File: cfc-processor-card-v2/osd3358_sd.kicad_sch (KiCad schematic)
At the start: 77 parts, among them J100 DM3BT-DSF-PEJS, U11 TCAN330, U17 25AAXX, U2 DS90CR218AMTD/NOPBMTD48_TEX-L, U3 THGBMJG7C2LBAU8, U7 OSD3358-512M-BSM

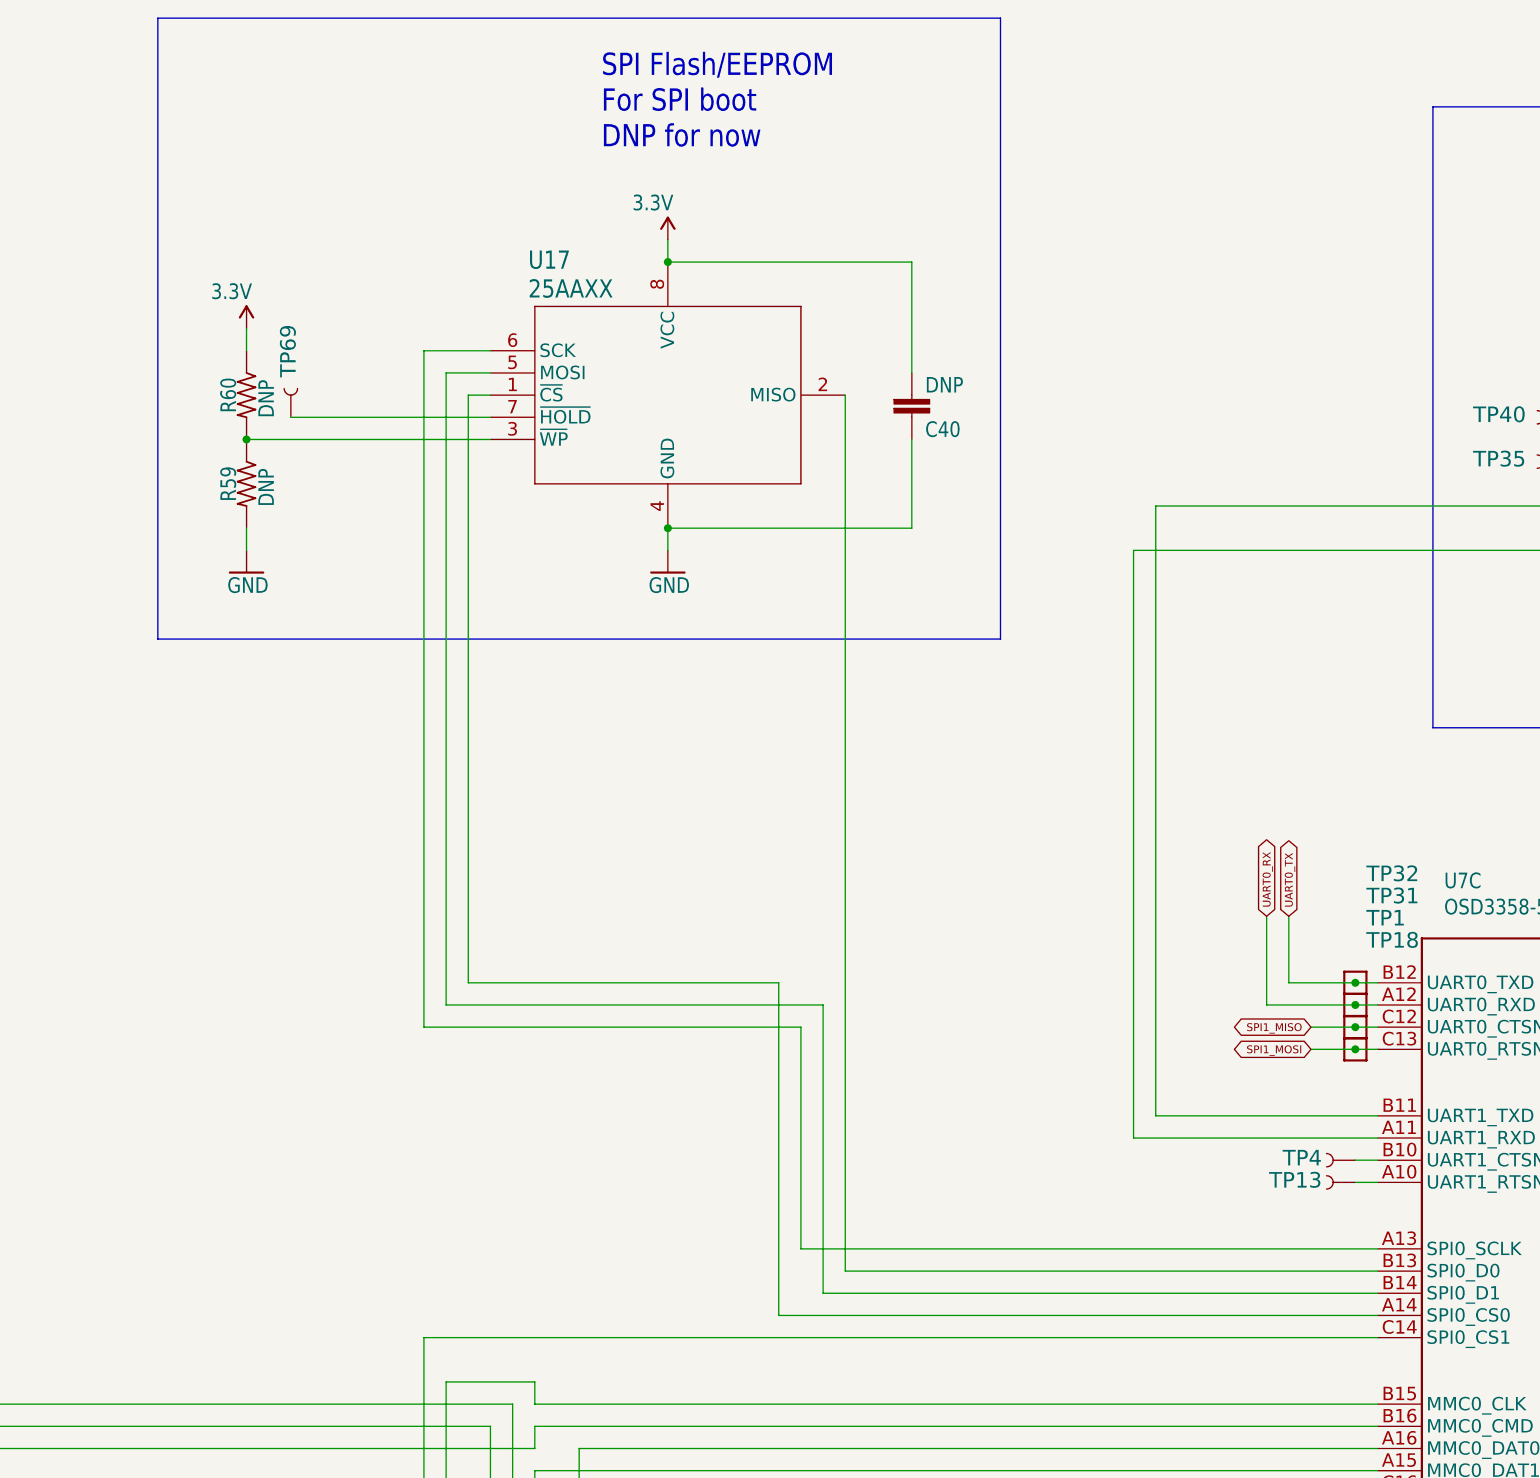
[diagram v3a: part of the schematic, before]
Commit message: More layout polishing Removed unused SPI EEPROM.
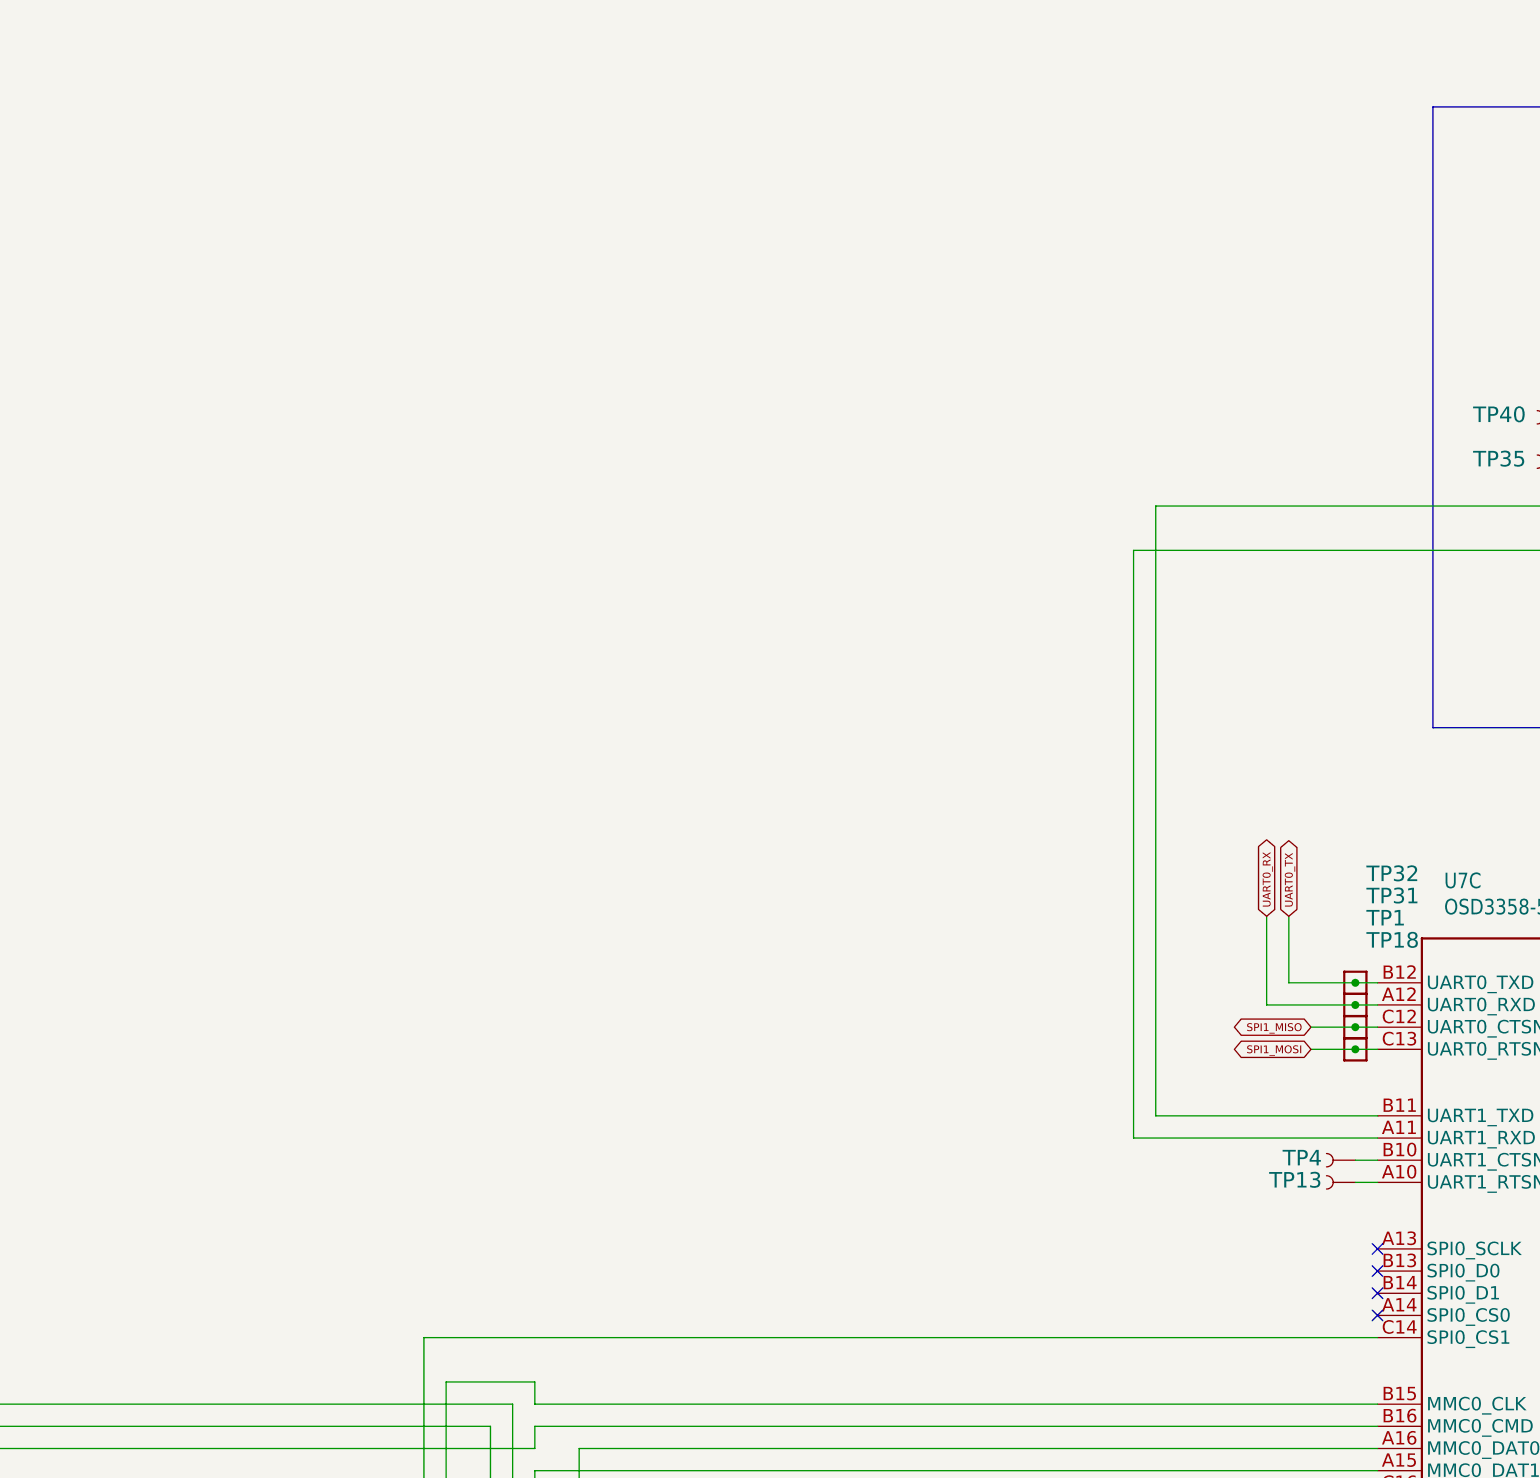
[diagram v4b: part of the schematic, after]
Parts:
- removed C40: DNP, oresat-passives:0603-C-NOSILK, symbol cfc-card-eagle-import:C-EU0603-A
- removed R59, R60: DNP, oresat-passives:0603-C-NOSILK, symbol cfc-card-eagle-import:R-US_0603-A
- removed TP69: TEST-POINT3X4, cfc-card:PAD.03X.04, symbol cfc-card-eagle-import:TEST-POINT3X4
- removed U17: 25AAXX, cfc-card:SOIC8, symbol cfc-card-eagle-import:25AAXX
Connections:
- no-connect marks 44 -> 48
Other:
- note removed: "SPI Flash/EEPROM For SPI boot DNP for now"

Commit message: Final polish on schematic and PCB. Cleaned up BOM, fixed github issues which were not really issues. Lots of BOM cleanup, with MPNs and DPNs.
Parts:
- removed TP33, TP34: TEST-POINT, cfc-card:2MM-TEST-POINT, symbol cfc-card-eagle-import:TEST-POINT
- added TP10, TP11, TP14, TP9: TEST-POINT3X4, cfc-card:PAD.03X.04, symbol cfc-card-eagle-import:TEST-POINT3X4
- C1, C16, C17, C20, C28, C7: DIS Digi-Key -> DigiKey; DPN 490-6350-1-ND -> 399-C0402C102J3GACAUTOCT-ND; MFR Murata -> KEMET; MPN GRM155R71H102KA01J -> C0402C102J3GACAUTO
- C10, C12, C3, C5, C6, C9: value 1uF -> 1u; DIS (none) -> DigiKey; DPN (none) -> 587-3473-1-ND; MFR (none) -> Taiyo Yuden; MPN (none) -> TMK107BJ105KAHT
- C11, C31: value 0.1uF -> 100n; DIS (none) -> DigiKey; DPN (none) -> 587-3472-1-ND; MFR (none) -> Taiyo Yuden; MPN (none) -> TMK107BJ104KAHT
- C2, C8: value 10uF -> 10u; DIS (none) -> DigiKey; DPN (none) -> 490-GRT21BC71E106KE13LCT-ND; MFR (none) -> Murata Electronics; MPN (none) -> GRT21BC71E106KE13L
- C21, C23, C24, C25, C26, C27: DIS Digi-Key -> DigiKey; DPN 399-7842-1-ND -> 399-C0402C100F5GACAUTOCT-ND; MFR Kemet -> KEMET; MPN C0603C103M5RACTU -> C0402C100F5GACAUTO
- C42, C43, C45, C46, C47, C48: DIS Digi-Key -> DigiKey; DPN 399-1177-1-ND -> 399-17167-1-ND; MFR Kemet -> KEMET; MPN C0805C104Z5VACTU -> C0402C104K4RECAUTO
- C49: footprint oresat-passives:0603-C-NOSILK -> oresat-passives:0805-C-NOSILK; DIS Digi-Key -> DigiKey; DPN 490-14372-1-ND -> 490-GRT21BC71E106KE13LCT-ND; MFR Murata -> Murata Electronics; MPN GRM188R61A106KE69J -> GRT21BC71E106KE13L
- D2, D3, D4, D5: footprint cfc-card:LED-0603 -> LED_SMD:LED_0603_1608Metric; symbol cfc-card-eagle-import:LED-BLUE0603 -> Device:LED_Small; DIS (none) -> DigiKey; DPN (none) -> 732-4966-1-ND; MFR (none) -> Wurth; MPN (none) -> 150060BS75000
- J6: renamed from J100; footprint cfc-card:DM3BT-DSF-PEJS -> oresat-connectors:J-Hirose-DM3BT-DSF-PEJS; symbol cfc-card-eagle-import:DM3BT-DSF-PEJS -> oresat-connectors:DM3BT-DSF-PEJS; DIS (none) -> DigiKey; DPN (none) -> HR1942CT-ND; MFR (none) -> Hirose; MPN (none) -> DM3BT-DSF-PEJS
- JP1, TP1, TP13, TP18, TP19, TP20, TP21, TP22, TP23, TP24, TP26, TP27, TP28, TP29, TP30, TP31, TP32, TP35, TP4, TP40: now left out of the parts list
- R11: value DNP -> 10k; now not fitted
- R2, R3, R4, R5: DIS (none) -> DigiKey; DPN (none) -> RMCF0603FT1K00CT-ND; MFR (none) -> Stackpole Electronics Inc; MPN (none) -> RMCF0603FT1K00
- R29, R30: value NP -> 100; now not fitted
- R6, R7: DIS Dgi-Key -> DigiKey; DPN 311-100MCT-ND -> RMCF0402FT100RCT-ND; MFR Yageo -> Stackpole Electronics Inc; MPN RC0201FR-07100RL -> RMCF0402FT100R
- RA1: renamed from R8; DIS (none) -> DigiKey; MFR (none) -> Panasonic Electronic Components; MPN (none) -> EXB-A10P103J
- RA2: renamed from R9; DIS (none) -> DigiKey; MFR (none) -> Panasonic Electronic Components; MPN (none) -> EXB-A10P103J
- RA3: renamed from R10; DIS (none) -> DigiKey; MFR (none) -> Panasonic Electronic Components; MPN (none) -> EXB-A10P103J
- U11: footprint cfc-card:SOT23-8_TI-DCN -> Package_TO_SOT_SMD:SOT-23-8; symbol cfc-card-eagle-import:TCAN330 -> oresat-ics:TCAN330; DIS (none) -> DigiKey; DPN (none) -> 296-44211-1-ND; MFR (none) -> Texas Instruments; MPN (none) -> TCAN330GDCNT
- U2: value DS90CR218AMTD/NOPBMTD48_TEX-L -> DS90CR218AMTD/NOPB; DIS (none) -> DigiKey; DPN (none) -> DS90CR218AMTD/NOPB-ND; MFR (none) -> Texas Instruments; MPN (none) -> DS90CR218AMTD/NOPB
- U3: value THGBMJG7C2LBAU8 -> SFEM016GB1EA1TO-I-GE-121-STD; DIS (none) -> DigiKey; DPN THGBMJG7C2LBAU8-ND -> 1052-SFEM016GB1EA1TO-I-GE-121-STD-ND; MFR (none) -> Swissbit; MPN THGBMJG7C2LBAU8 -> SFEM016GB1EA1TO-I-GE-121-STD
- U7: value OSD3358-512M-BSM -> OSD3358-1G-ISM; footprint cfc-card:OSD335X-BGA-256 -> oresat-ics:U-Octavo-OSD335X-BGA-256; symbol cfc-card-eagle-import:OSD3358-512M-BSM -> oresat-ics:OSD3358-512M-BSM; DIS (none) -> DigiKey; DPN (none) -> 1676-OSD3358-1G-ISM-ND; MFR (none) -> Octavo Systems; MPN (none) -> OSD3358-1G-ISM
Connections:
- net GND: now also D2.1 (K), D3.1 (K), D4.1 (K), D5.1 (K); no longer D2.C, D3.C, D4.C, D5.C
- net at R2.2: now also D2.2 (A); no longer D2.A
- net EMMC_D0: now reaches RA2.6 (66), U3.A3 (D0), U7.R3 (GPMC_AD0)
- net EMMC_D1: now reaches RA3.1 (11), U3.A4 (D1), U7.R2 (GPMC_AD1)
- net EMMC_D2: now reaches RA3.9 (99), U3.A5 (D2), U7.R1 (GPMC_AD2)
- net EMMC_D3: now reaches RA2.4 (44), U3.B2 (D3), U7.T3 (GPMC_AD3)
- net EMMC_D4: now reaches RA2.7 (77), U3.B3 (D4), U7.T2 (GPMC_AD4)
- net EMMC_D5: now reaches RA2.8 (88), U3.B4 (D5), U7.T1 (GPMC_AD5)
- net EMMC_D6: now reaches RA3.8 (88), U3.B5 (D6), U7.P4 (GPMC_AD6)
- net EMMC_D7: now reaches RA3.2 (22), U3.B6 (D7), U7.R4 (GPMC_AD7)
- net at R3.2: now also D3.2 (A); no longer D3.A
- net at R5.2: now also D5.2 (A); no longer D5.A
- net at R4.2: now also D4.2 (A); no longer D4.A
- net at U7.P7 (GPMC_AD15): now also TP14.P$1 (1)
- net at U7.T6 (GPMC_AD14): now also TP11.P$1 (1)
- net PRU_BUS.PRU0_14: no longer names the net of U7.P6 (GPMC_AD12)
- net PRU_BUS.PRU0_14: now also TP9.P$1 (1)
- net PRU_BUS.PRU0_15: no longer names the net of U7.R6 (GPMC_AD13)
- net PRU_BUS.PRU0_15: now also TP10.P$1 (1)
- no-connect marks 48 -> 46
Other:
- note removed: "CAN1 RX --> B11 --> UART1_TXD CAN1 TX --> A11 --> UART1_RXD"
- moved on the sheet: C1, C10, C11, C12, C16, C17, C2, C20, C21, C23, C24, C25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
